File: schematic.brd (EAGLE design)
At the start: 100 x 70 mm, 23 parts, among them U1 ADP3338AKCZ-3.3RL7

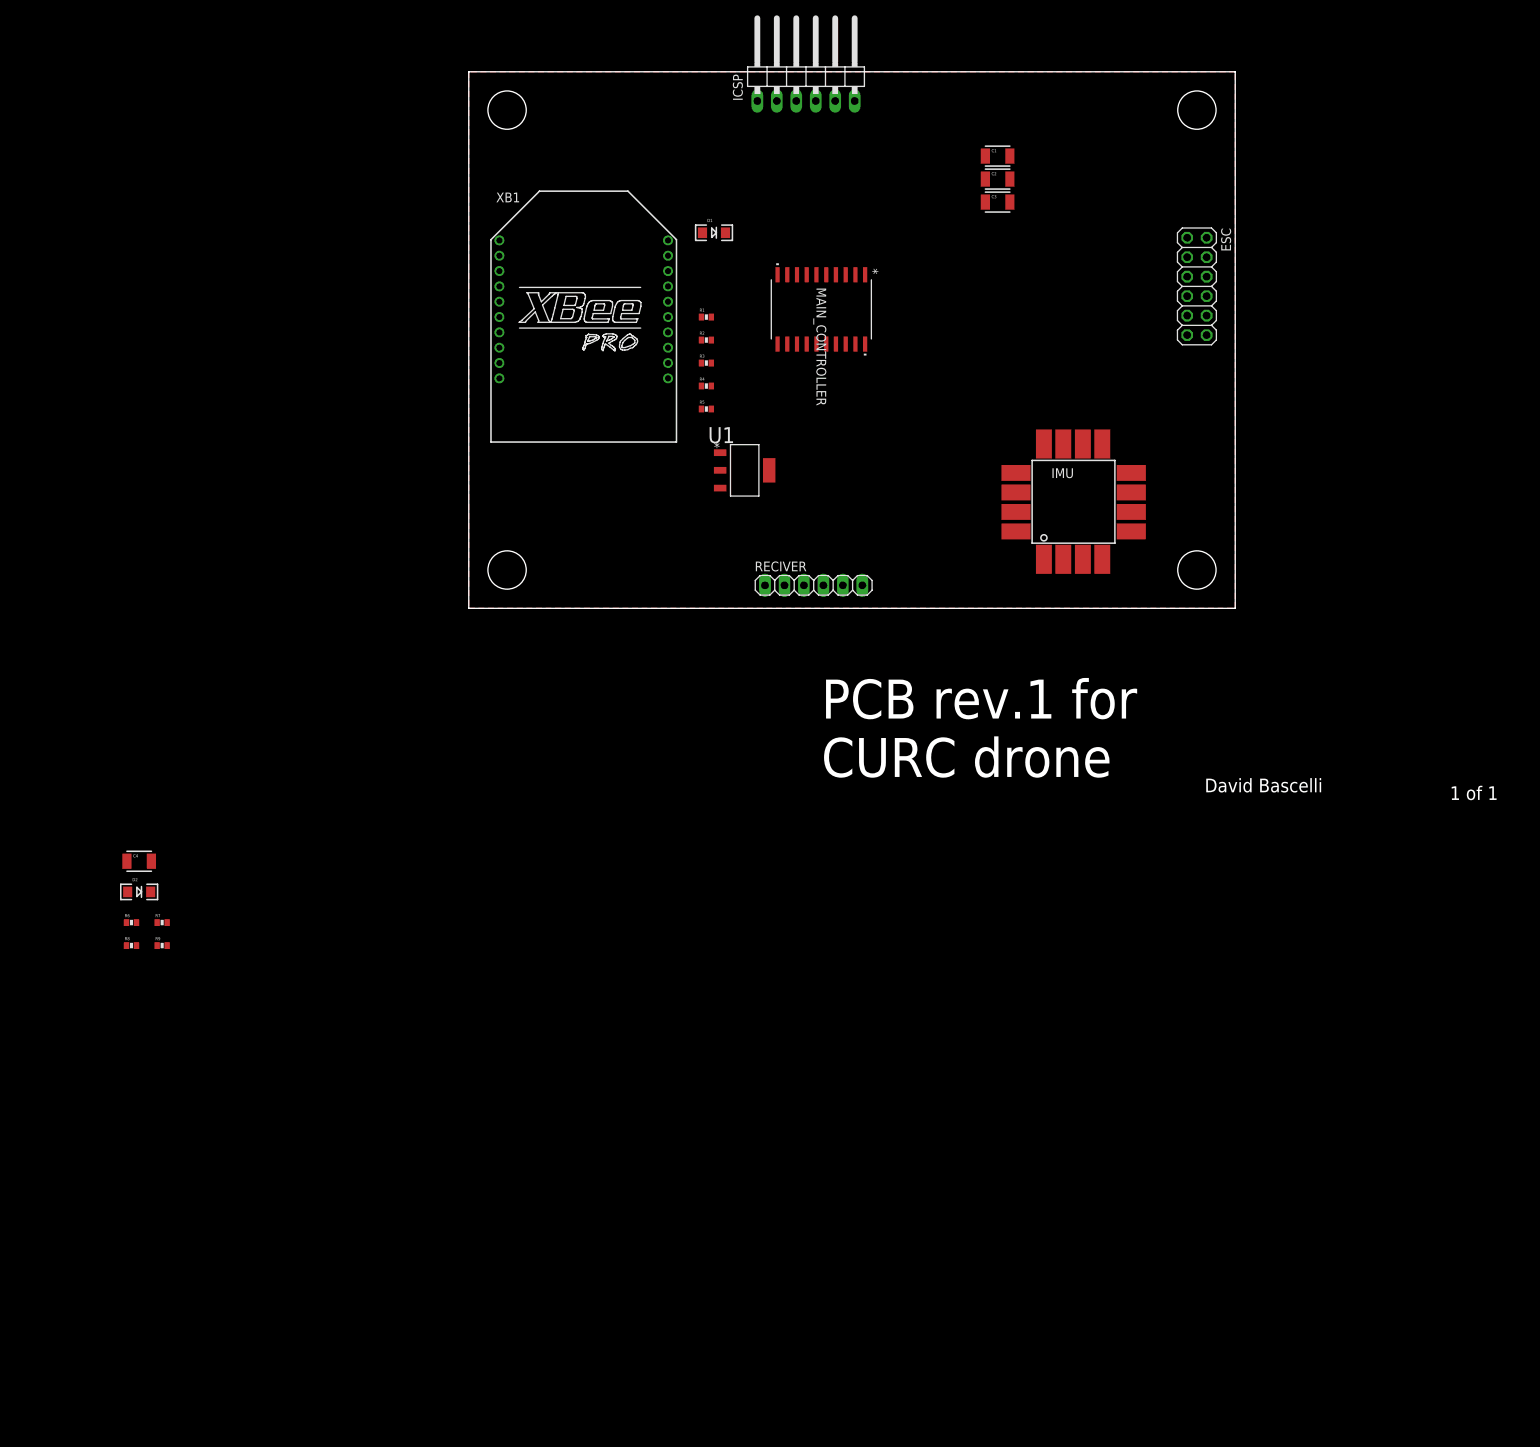
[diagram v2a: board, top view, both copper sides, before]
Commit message: Added missing connections for IMU and XBEE. Added inturrupt pin for XBEE.
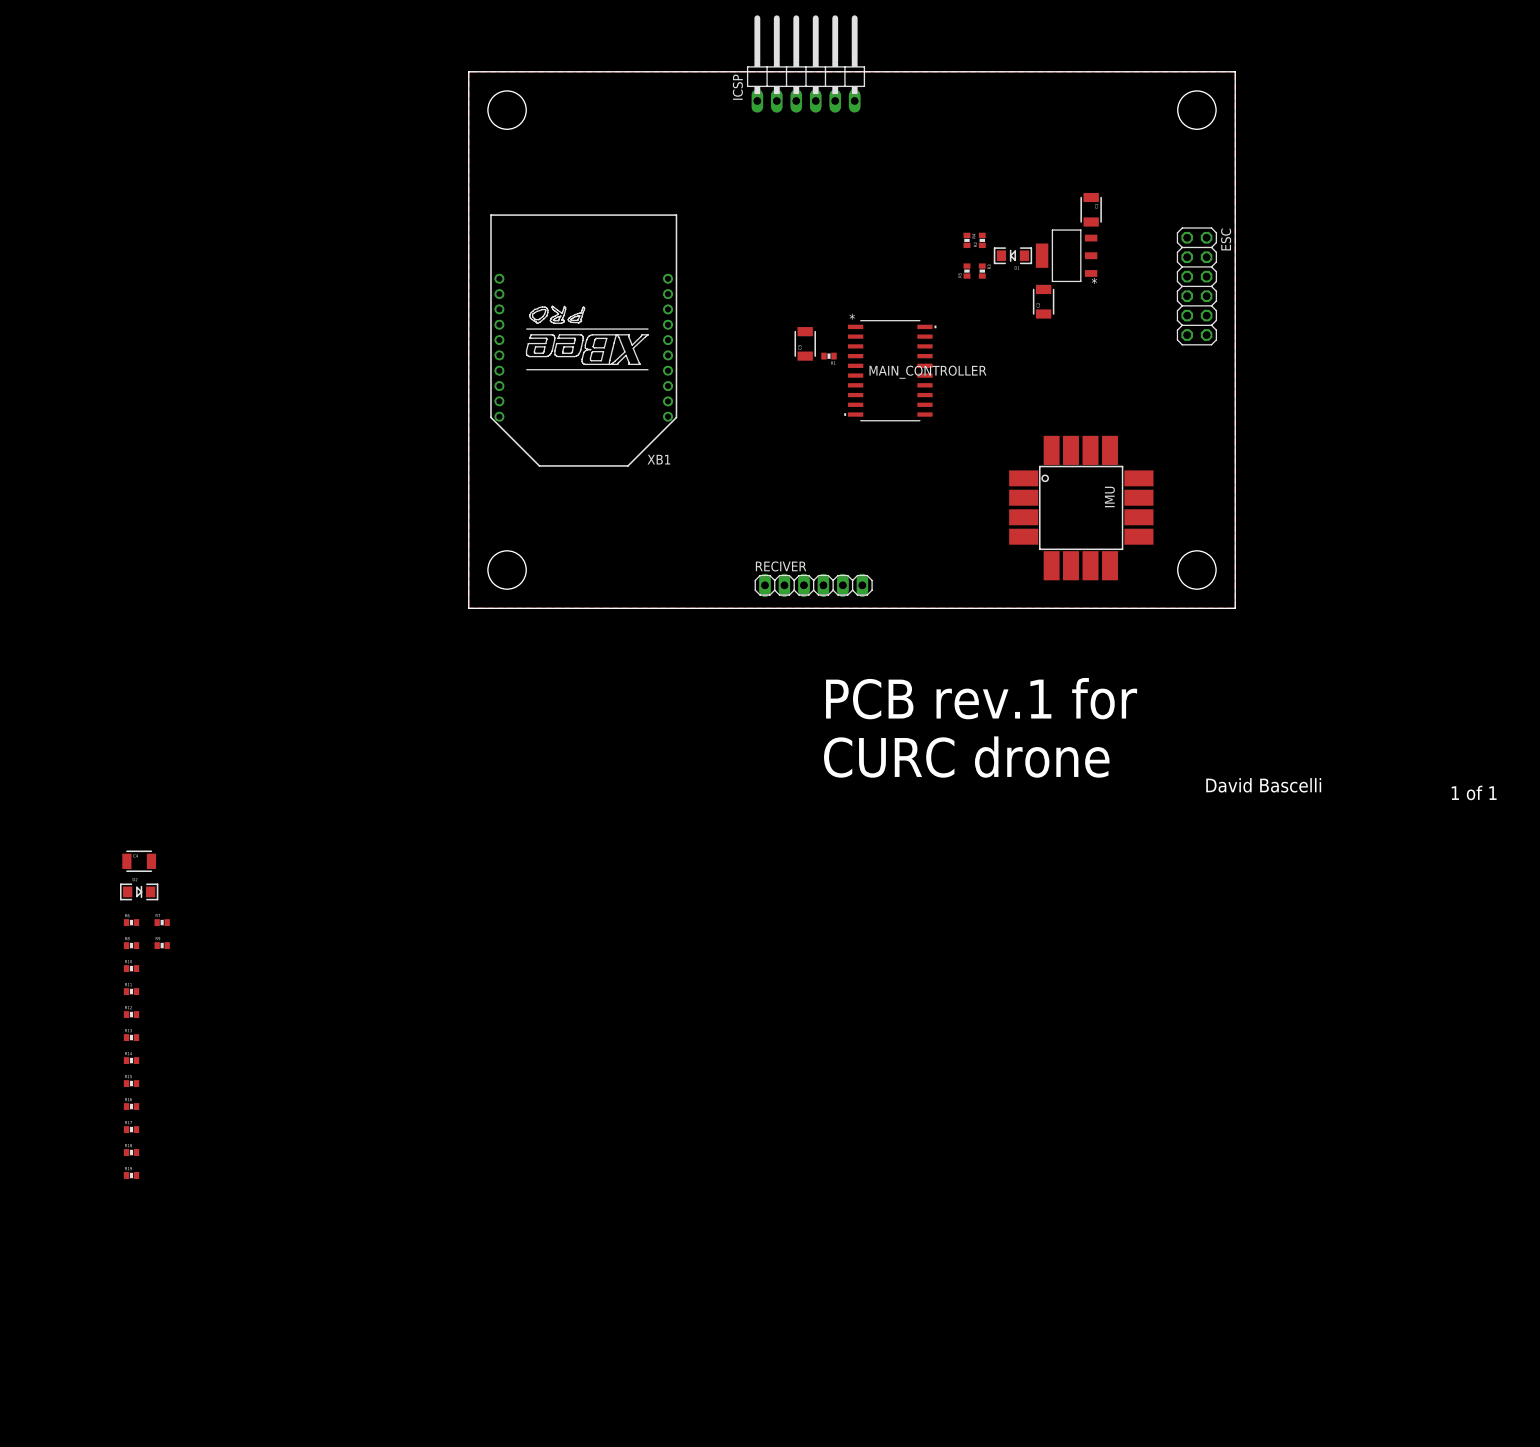
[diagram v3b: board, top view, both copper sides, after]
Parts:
- added R10, R11, R12, R13, R14, R15, R16, R17, R18, R19: 10k, SparkFun-Passives:0402-RES
- moved U1 50.5 mm to (78.0, 46.0), turned to 180 degrees
- moved D1 39.1 mm to (71.0, 46.0), turned to 180 degrees
- moved R4 38.9 mm to (65.0, 48.0), turned to 270 degrees
- moved R5 38.5 mm to (65.0, 44.0), turned to 90 degrees
- moved R2 38.3 mm to (67.0, 48.0), turned to 90 degrees
- moved R3 37.9 mm to (67.0, 44.0), turned to 270 degrees
- moved C3 31.2 mm to (43.9, 34.5), turned to 90 degrees
- moved C2 17.1 mm to (75.0, 40.0), turned to 90 degrees
- moved IMU 17.0 mm to (71.0, 22.0), turned to 270 degrees
- moved R1 16.8 mm to (47.0, 32.9), turned to 180 degrees
- moved C1 14.1 mm to (81.2, 52.0), turned to 270 degrees
- moved MAIN_CONTROLLER 12.0 mm to (55.0, 31.0), turned to 0 degrees
- moved XB1 5.00 mm to (15.0, 34.0), turned to 180 degrees
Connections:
- new net IMU_WAKE: IMU.P$1, MAIN_CONTROLLER.8
- new net N$10: IMU.P$11, R10.2
- new net N$11: R10.1, R11.2
- new net N$12: R11.1, R12.2
- new net N$13: R12.1, R13.2
- new net N$14: R13.1, R14.1
- new net N$15: R14.2, R15.1
- new net N$16: R15.2, R16.1
- new net N$17: R16.2, R17.1
- new net N$18: R17.2, R18.1
- new net N$19: R18.2, R19.1
- new net XBEE_INT: MAIN_CONTROLLER.16, XB1.4
- net VCC: now also XB1.14
- net VDD: now also R19.2
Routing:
- added copper zone on layer 1, net GND
- removed copper zone on layer 1, net N$1

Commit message: Inital placement of components
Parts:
- moved R19 165.6 mm to (95.0, 16.0), turned to 180 degrees
- moved R18 165.1 mm to (95.0, 18.0)
- moved R17 164.5 mm to (95.0, 20.0), turned to 180 degrees
- moved R16 164.0 mm to (95.0, 22.0)
- moved R15 162.1 mm to (93.3, 24.1)
- moved R14 158.3 mm to (92.0, 22.0)
- moved R13 155.8 mm to (92.0, 20.0)
- moved R12 153.4 mm to (92.0, 18.0), turned to 180 degrees
- moved R11 151.2 mm to (92.0, 16.0)
- moved R10 149.1 mm to (91.9, 14.4), turned to 180 degrees
- moved R9 116.3 mm to (12.0, 60.0)
- moved R8 115.5 mm to (12.0, 57.0)
- moved R7 111.8 mm to (8.00, 60.0)
- moved R6 110.9 mm to (8.00, 57.0)
- moved D2 103.3 mm to (4.00, 55.0), turned to 90 degrees
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
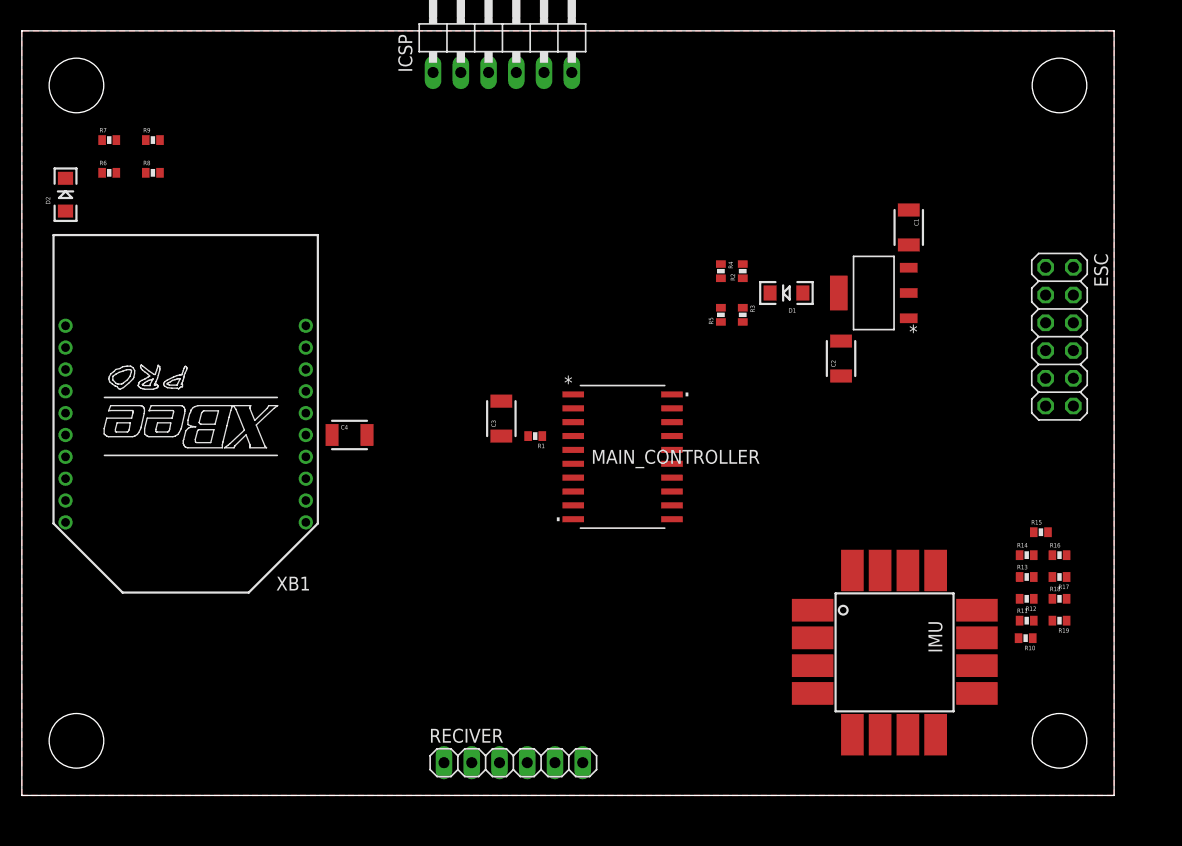
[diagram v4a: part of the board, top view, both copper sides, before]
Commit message: Inital laying of all traces. Jumpers still need to be added
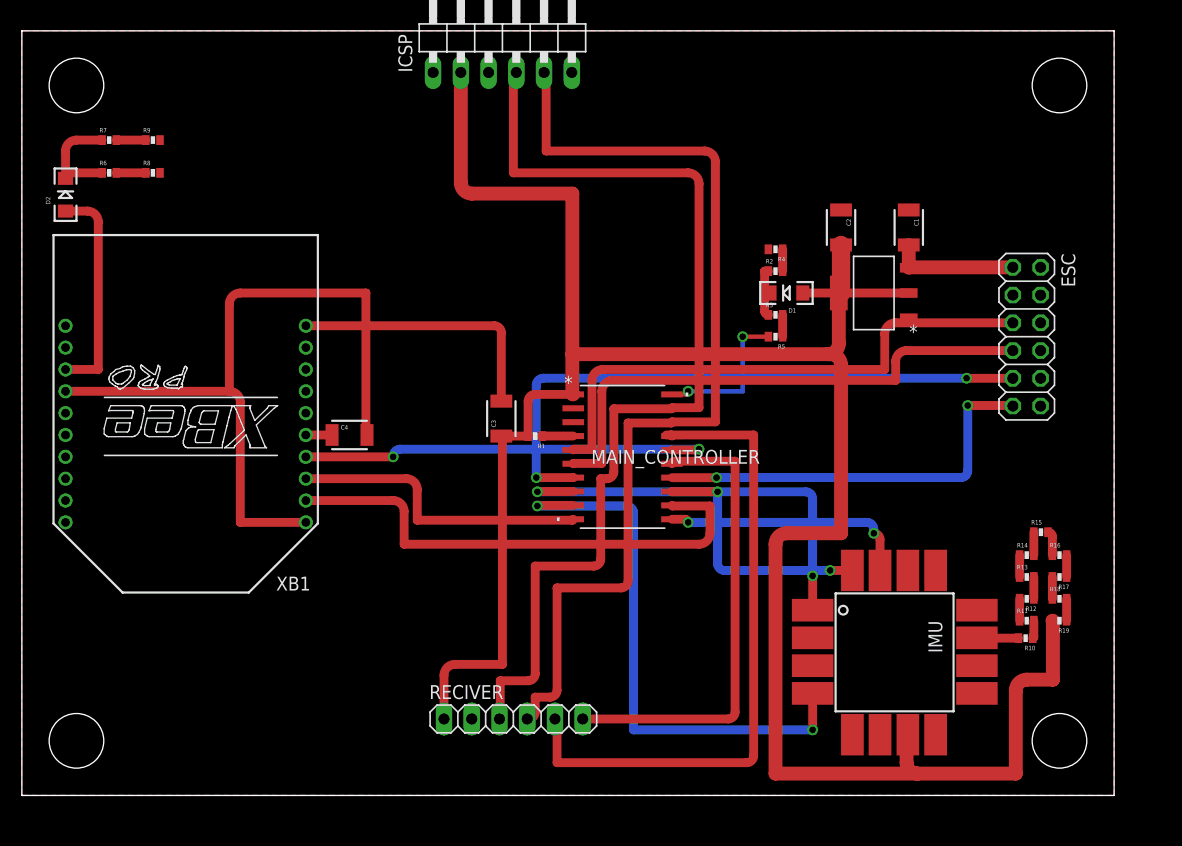
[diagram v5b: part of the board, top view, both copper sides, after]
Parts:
- moved C2 12.0 mm to (75.0, 52.0), turned to 270 degrees
- moved R4 5.39 mm to (69.0, 50.0), turned to 180 degrees
- moved R5 5.39 mm to (69.0, 42.0), turned to 180 degrees
- moved RECIVER 4.00 mm to (45.0, 7.00)
- moved ESC 3.00 mm to (92.0, 42.0)
- moved R2 3.00 mm to (69.0, 48.0), turned to 0 degrees
- moved R3 3.00 mm to (69.0, 44.0), turned to 0 degrees
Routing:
- net VDD: track 0.00 -> 211.2 mm
- net PGD/PITCH: track 0.00 -> 92.8 mm
- net PGC/ROLL: track 0.00 -> 90.2 mm
- net VCC: track 0.00 -> 67.4 mm
- net YAW: track 0.00 -> 59.8 mm
- net M3: track 0.00 -> 55.7 mm, vias 0 -> 2
- net IMU_INT: track 0.00 -> 52.0 mm, vias 0 -> 2
- net M1: track 0.00 -> 50.7 mm
- net M2: track 0.00 -> 49.4 mm
- net RX: track 0.00 -> 46.8 mm
- net THROTTLE: track 0.00 -> 43.1 mm
- net IMU_WAKE: track 0.00 -> 39.0 mm, vias 0 -> 2
- net XBEE_INT: track 0.00 -> 38.8 mm, vias 0 -> 2
- net GND: track 0.00 -> 38.5 mm, vias 0 -> 2
- net M4: track 0.00 -> 37.5 mm, vias 0 -> 2
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
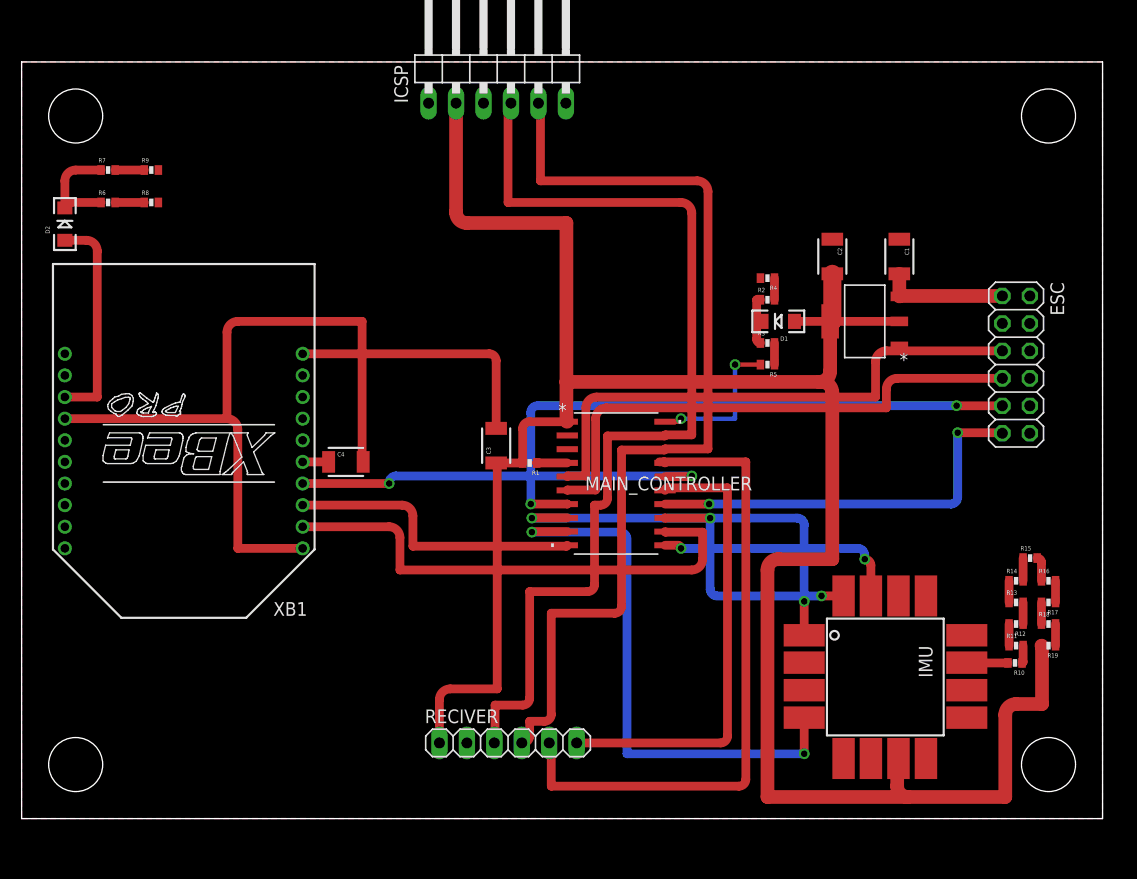
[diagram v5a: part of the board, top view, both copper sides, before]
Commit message: Repositioned components to reduce number of jumber cables needed
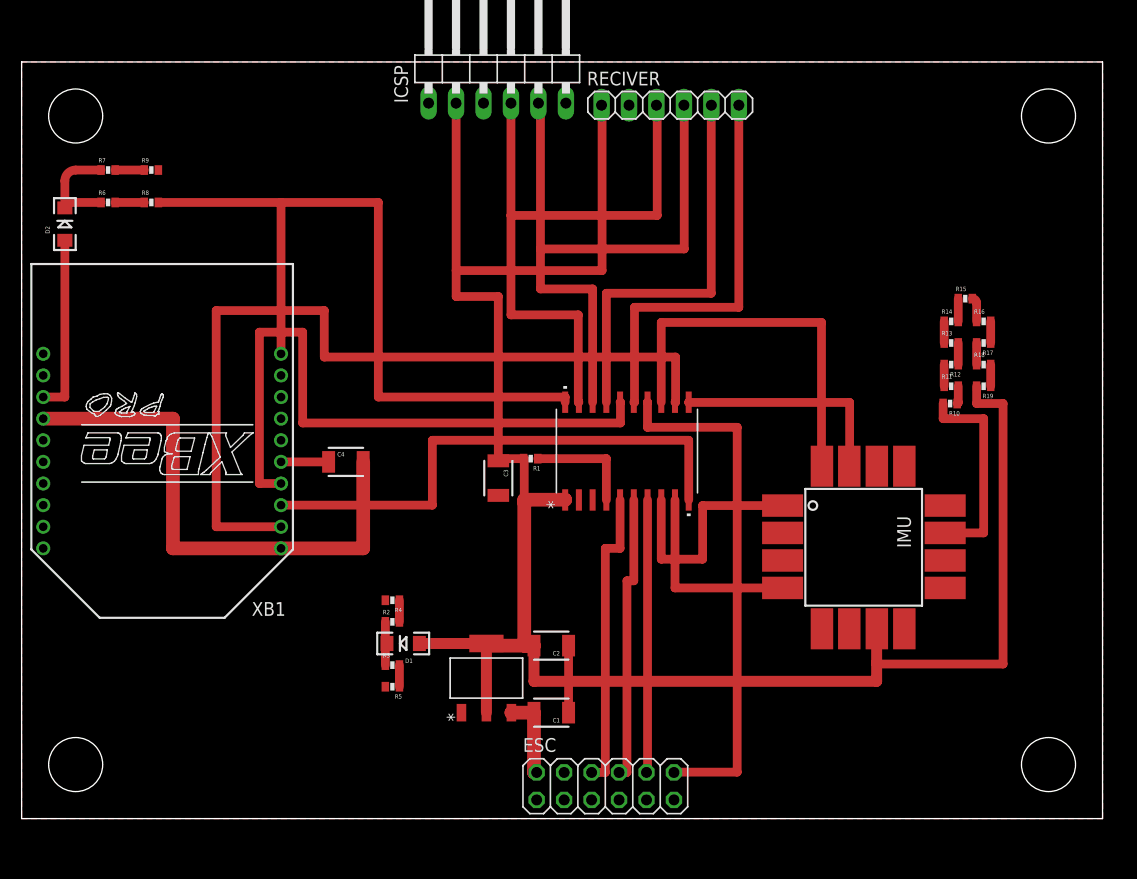
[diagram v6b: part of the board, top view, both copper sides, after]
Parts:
- moved RECIVER 60.9 mm to (60.0, 66.0)
- moved ESC 54.5 mm to (54.0, 3.00), turned to 0 degrees
- moved C1 53.1 mm to (49.0, 9.80), turned to 180 degrees
- moved U1 48.1 mm to (43.0, 13.0), turned to 90 degrees
- moved D1 45.7 mm to (35.3, 16.2)
- moved R2 45.7 mm to (34.3, 18.2)
- moved R3 45.7 mm to (34.3, 14.2)
- moved R4 45.7 mm to (34.3, 20.2)
- moved R5 45.7 mm to (34.3, 12.2)
- moved C2 44.4 mm to (49.0, 16.0), turned to 180 degrees
- moved R10 24.7 mm to (85.9, 38.4)
- moved R11 24.7 mm to (86.0, 40.0)
- moved R12 24.7 mm to (86.0, 42.0)
- moved R13 24.7 mm to (86.0, 44.0)
- moved R14 24.7 mm to (86.0, 46.0)
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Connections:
- net 5V: now also ESC.2; no longer ESC.1
- net GND: now also ESC.4; no longer ESC.3
- net M1: now also ESC.6; no longer ESC.5
- net M2: now also ESC.8; no longer ESC.7
- net M3: now also ESC.10; no longer ESC.9
- net M4: now also ESC.12; no longer ESC.11
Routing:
- net GND: track 38.5 -> 76.0 mm, vias 2 -> 0
- net PGD/PITCH: track 92.8 -> 57.8 mm
- net IMU_INT: track 52.0 -> 18.1 mm, vias 2 -> 0
- net PGC/ROLL: track 90.2 -> 59.3 mm
- net M3: track 55.7 -> 25.3 mm, vias 2 -> 0
- net RX: track 46.8 -> 77.0 mm
- net VDD: track 211.2 -> 187.6 mm
- net M2: track 49.4 -> 26.6 mm
- net M1: track 50.7 -> 27.8 mm
- net YAW: track 59.8 -> 37.2 mm
- net TX: track 27.7 -> 49.2 mm
- net XBEE_INT: track 38.8 -> 59.8 mm, vias 2 -> 0
- net VCC: track 67.4 -> 49.6 mm
- net IMU_WAKE: track 39.0 -> 21.7 mm, vias 2 -> 0
- net N$10: track 3.82 -> 19.3 mm
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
